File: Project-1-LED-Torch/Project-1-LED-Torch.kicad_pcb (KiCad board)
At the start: 2 copper layers, 4 parts, among them SW1 SW_DPDT_x2

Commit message: do PCB layout design, step 8, setup
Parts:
- moved BT1 4.82 mm to (139.0, 74.5)
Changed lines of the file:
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@@
 	(footprint "Battery:BatteryHolder_Keystone_1058_1x2032"
 		(layer "F.Cu")
-		(at 138.975 79.32397)
+		(at 138.975 74.5)
 		(descr "http://www.keyelco.com/product-pdf.cfm?p=14028")
 		(tags "Keystone type 1058 coin cell retainer")

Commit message: do PCB layout design, steps 9, 10, outline and constraints, footprints
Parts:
- moved D1 90.4 mm to (56.2, 113.2)
- moved SW1 63.2 mm to (73.5, 111.0)
- moved R1 59.2 mm to (69.2, 117.1), turned to 90 degrees
- moved BT1 55.9 mm to (98.8, 113.2)
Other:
- board outline added: 62.5 x 18.5 mm
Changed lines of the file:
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@@
 	(footprint "LED_THT:LED_D5.0mm"
 		(layer "F.Cu")
-		(at 144.785 95.375)
+		(at 56.21 113.25)
 		(descr "LED, diameter 5.0mm, 2 pins, http://cdn-reichelt.de/documents/datenblatt/A500/LL-504BC2E-009.pdf, generated by kicad-footprint-generator")
 		(tags "LED")
@@
 		)
 		(point
-			(at 146.055 95.375)
+			(at 57.48 113.25)
 			(size 2)
 			(layer "F.Fab")
@@
 	(footprint "Button_Switch_THT:SW_TH_Tactile_Omron_B3F-100x"
 		(layer "F.Cu")
-		(at 134.195 93.265)
+		(at 73.5 111)
 		(descr "Tactile switch, 6x6 mm, H4.3 mm, 6.5 mm pitch, https://omronfs.omron.com/en_US/ecb/products/pdf/en-b3f.pdf")
 		(tags "Omron B3F-10xx SPST 1P1T")
@@
 	(footprint "Resistor_THT:R_Axial_DIN0204_L3.6mm_D1.6mm_P7.62mm_Horizontal"
 		(layer "F.Cu")
-		(at 123.475 93.215)
+		(at 69.25 117.06 90)
 		(descr "Resistor, Axial_DIN0204 series, Axial, Horizontal, pin pitch=7.62mm, 0.167W, length*diameter=3.6*1.6mm^2, http://cdn-reichelt.de/documents/datenblatt/B400/1_4W%23YAG.pdf")
 		(tags "Resistor Axial_DIN0204 series Axial Horizontal pin pitch 7.62mm 0.167W length 3.6mm diameter 1.6mm")
 		(property "Reference" "R1"
-			(at 3.81 -1.92 0)
+			(at 3.81 -1.92 90)
 			(layer "F.SilkS")
 			(effects
@@
 		)
 		(property "Value" "R"
-			(at 3.81 1.92 0)
+			(at 3.81 1.92 90)
 			(layer "F.Fab")
 			(effects
@@
 		)
 		(property "Datasheet" ""
-			(at 0 0 0)
+			(at 0 0 90)
 			(layer "F.Fab")
 			(hide yes)
@@
 		)
 		(property "Description" "Resistor"
-			(at 0 0 0)
+			(at 0 0 90)
 			(layer "F.Fab")
 			(hide yes)
@@
 		)
 		(property "KiLib_Generator" "resistor/THT"
-			(at 0 0 0)
+			(at 0 0 90)
 			(layer "F.SilkS")
 			(hide yes)
@@
 		(duplicate_pad_numbers_are_jumpers no)
 		(fp_line
+			(start 6.68 0)
+			(end 5.73 0)
+			(stroke
+				(width 0.12)
+				(type solid)
+			)
+			(layer "F.SilkS")
+		)
+		(fp_line
 			(start 0.94 0)
 			(end 1.89 0)
-			(stroke
-				(width 0.12)
-				(type solid)
-			)
-			(layer "F.SilkS")
-		)
-		(fp_line
-			(start 6.68 0)
-			(end 5.73 0)
 			(stroke
 				(width 0.12)
@@
 		)
 		(fp_line
+			(start 7.62 0)
+			(end 5.61 0)
+			(stroke
+				(width 0.1)
+				(type solid)
+			)
+			(layer "F.Fab")
+		)
+		(fp_line
 			(start 0 0)
 			(end 2.01 0)
-			(stroke
-				(width 0.1)
-				(type solid)
-			)
-			(layer "F.Fab")
-		)
-		(fp_line
-			(start 7.62 0)
-			(end 5.61 0)
 			(stroke
 				(width 0.1)
@@
 		)
 		(fp_text user "${REFERENCE}"
-			(at 3.81 0 0)
+			(at 3.81 0 90)
 			(layer "F.Fab")
 			(effects
@@
 		)
 		(pad "1" thru_hole circle
-			(at 0 0)
+			(at 0 0 90)
 			(size 1.4 1.4)
 			(drill 0.7)
@@
 		)
 		(pad "2" thru_hole circle
-			(at 7.62 0)
+			(at 7.62 0 90)
 			(size 1.4 1.4)
 			(drill 0.7)
@@
 	(footprint "Battery:BatteryHolder_Keystone_1058_1x2032"
 		(layer "F.Cu")
-		(at 138.975 74.5)
+		(at 98.75 113.25)
 		(descr "http://www.keyelco.com/product-pdf.cfm?p=14028")
 		(tags "Keystone type 1058 coin cell retainer")
@@
 		)
 	)
+	(gr_rect
+		(start 53.5 104)
+		(end 116 122.5)
+		(stroke
+			(width 0.05)
+			(type default)
+		)
+		(fill no)
+		(layer "Edge.Cuts")
+	)
+	(gr_circle
+		(center 63.5 113.25)
+		(end 65 113.25)
+		(stroke
+			(width 0.05)
+			(type default)
+		)
+		(fill no)
+		(layer "Edge.Cuts")
+	)
 	(embedded_fonts no)

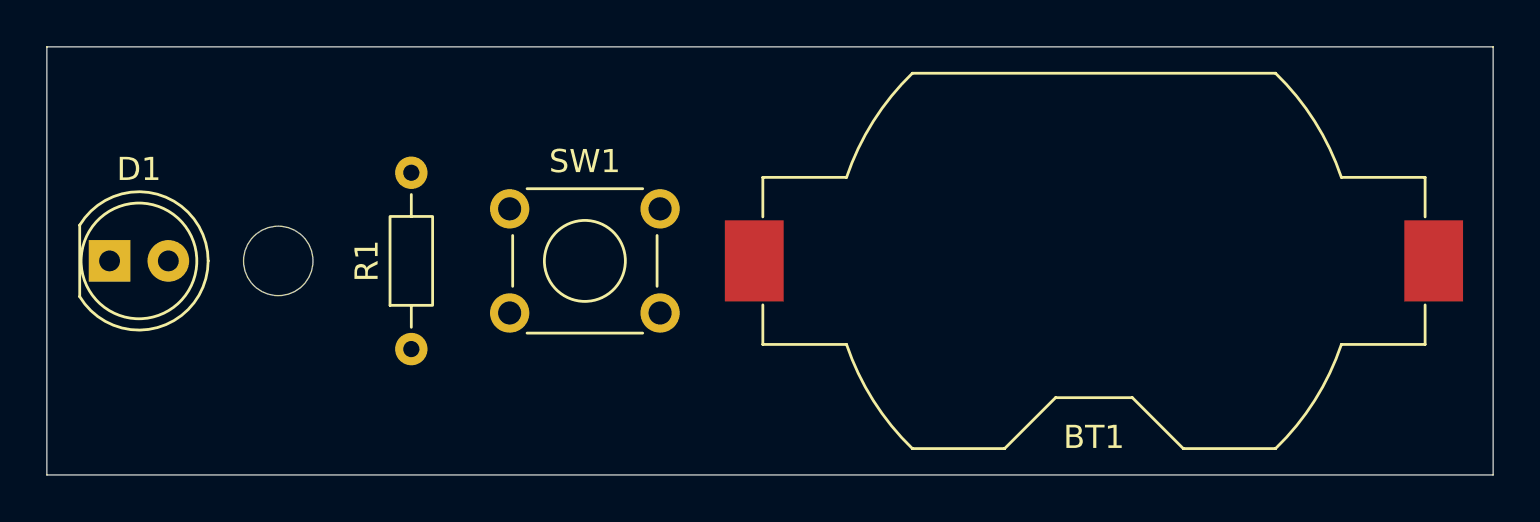
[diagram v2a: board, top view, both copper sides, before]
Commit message: minor update PCB layout design, steps 9, 10, outline and constraints, footprints
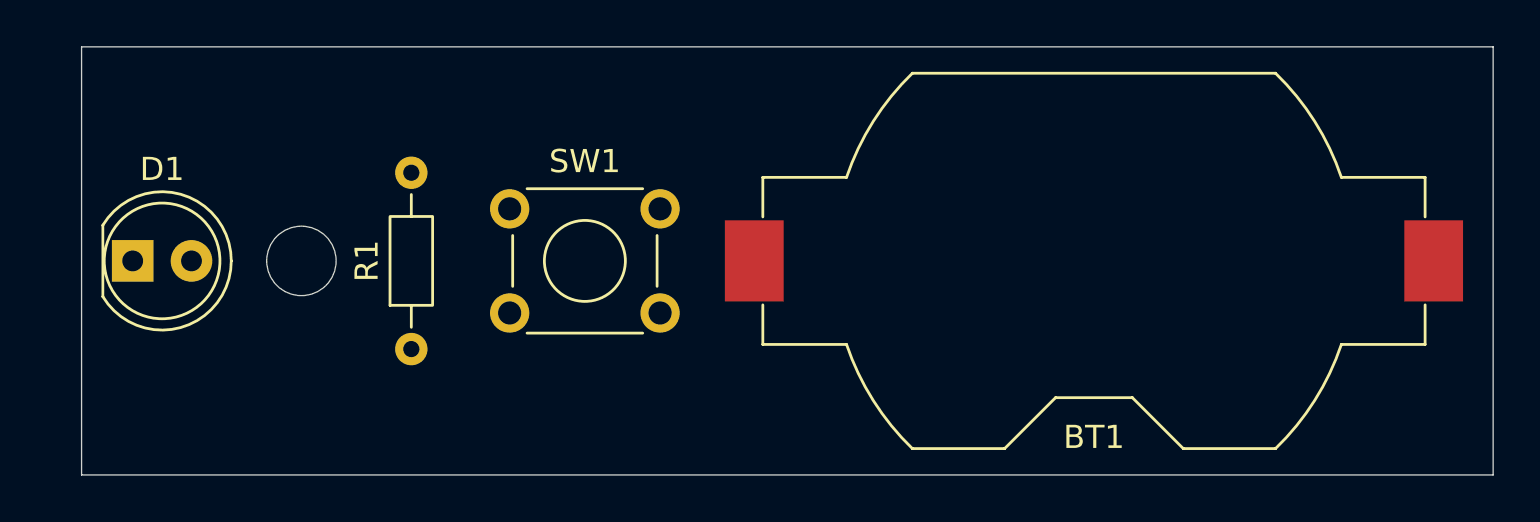
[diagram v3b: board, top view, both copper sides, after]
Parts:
- moved D1 1.00 mm to (57.2, 113.2)
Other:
- board size 62.5 x 18.5 mm -> 61 x 18.5 mm
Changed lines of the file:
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@@
 	(footprint "LED_THT:LED_D5.0mm"
 		(layer "F.Cu")
-		(at 56.21 113.25)
+		(at 57.21 113.25)
 		(descr "LED, diameter 5.0mm, 2 pins, http://cdn-reichelt.de/documents/datenblatt/A500/LL-504BC2E-009.pdf, generated by kicad-footprint-generator")
 		(tags "LED")
@@
 		)
 		(point
-			(at 57.48 113.25)
+			(at 58.48 113.25)
 			(size 2)
 			(layer "F.Fab")
@@
 	)
 	(gr_rect
-		(start 53.5 104)
+		(start 55 104)
 		(end 116 122.5)
 		(stroke
@@
 	)
 	(gr_circle
-		(center 63.5 113.25)
-		(end 65 113.25)
+		(center 64.5 113.25)
+		(end 66 113.25)
 		(stroke
 			(width 0.05)

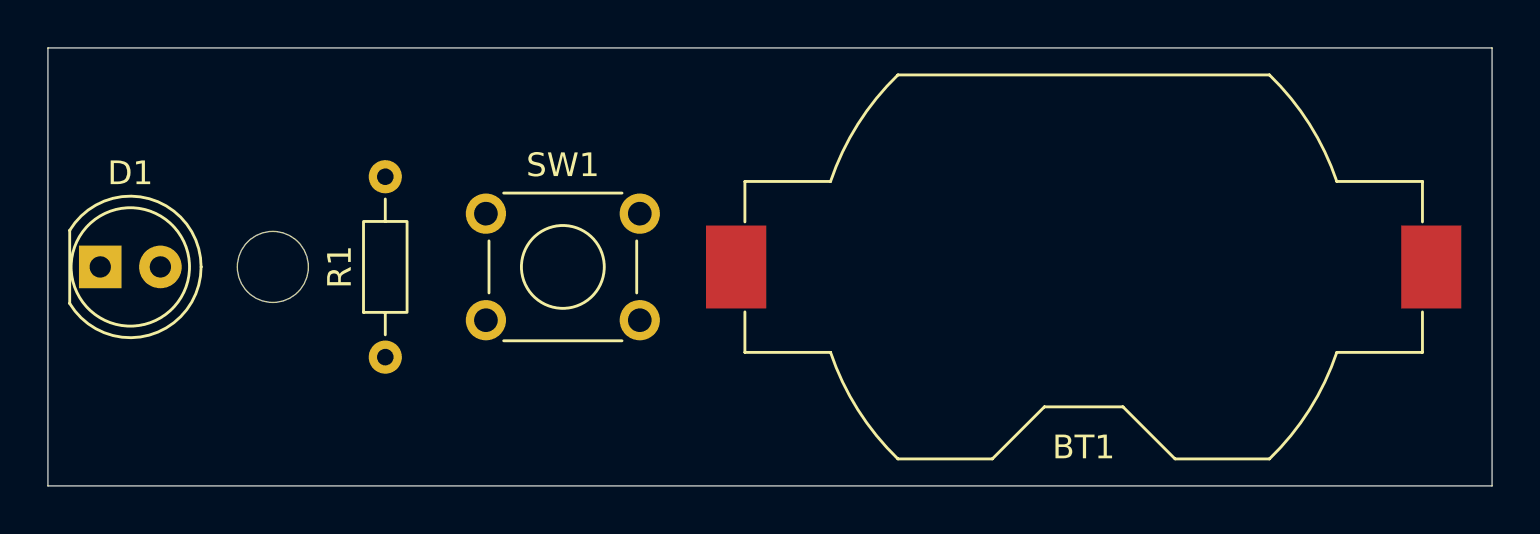
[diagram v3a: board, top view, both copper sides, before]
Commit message: do PCB layout design, step 11, route
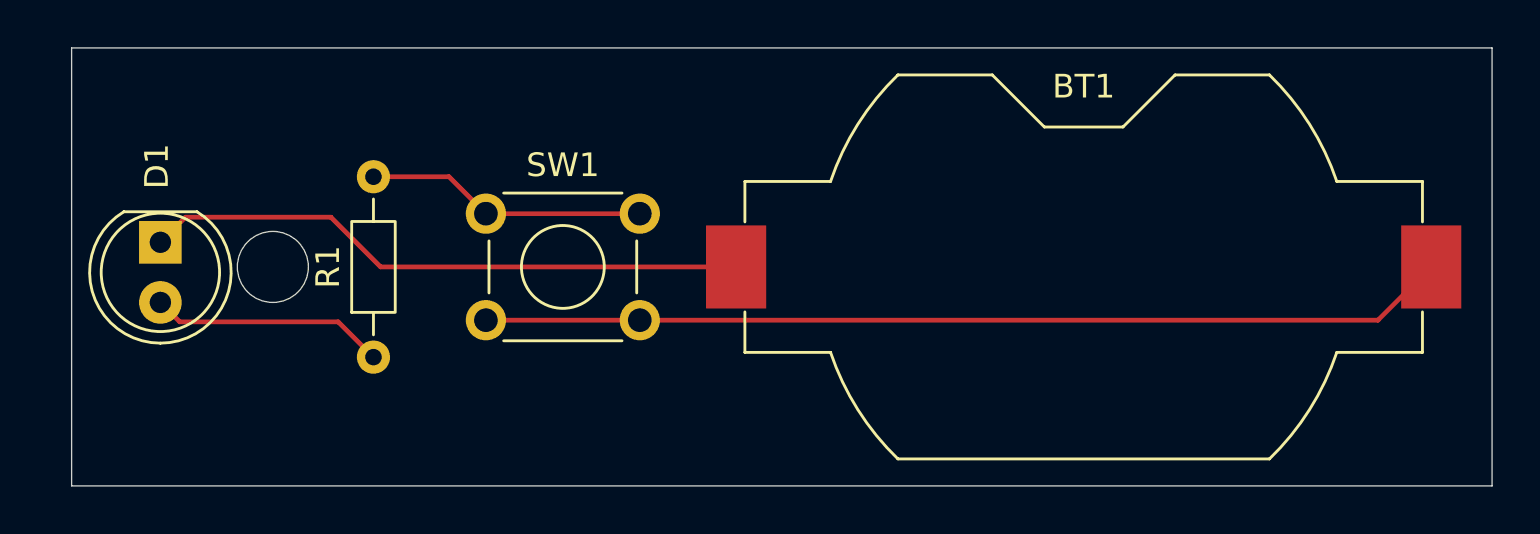
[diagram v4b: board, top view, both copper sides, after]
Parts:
- moved D1 2.74 mm to (59.8, 112.2), turned to -90 degrees
- moved R1 0.50 mm to (68.8, 117.1)
- turned BT1 to 180 degrees
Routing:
- net /Battery_positive: track 0.00 -> 40.9 mm
- net /LED_cathode: track 0.00 -> 25.6 mm
- net Net-(SW1A-A): track 0.00 -> 11.9 mm
- net /LED_anode: track 0.00 -> 9.96 mm
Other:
- board size 61 x 18.5 mm -> 60 x 18.5 mm

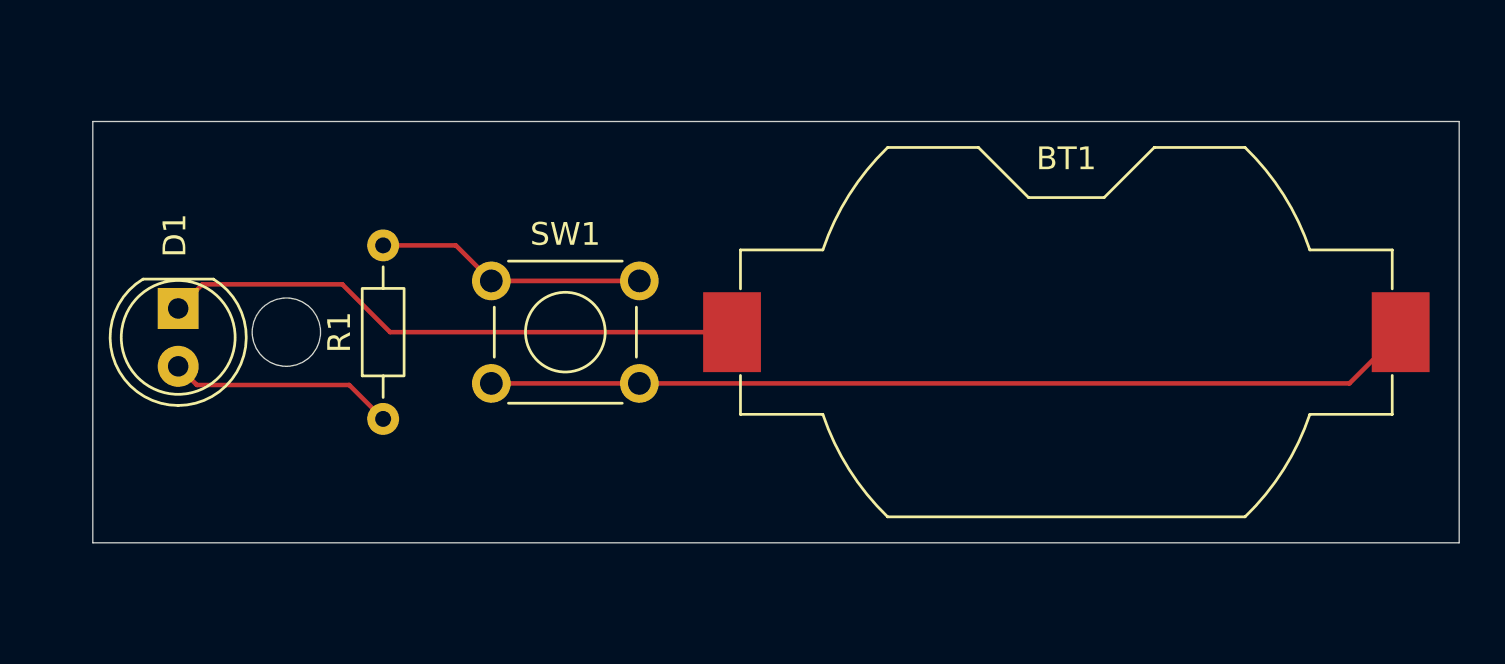
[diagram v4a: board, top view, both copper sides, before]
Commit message: update PCB layout design, steps 9 11, outline, route
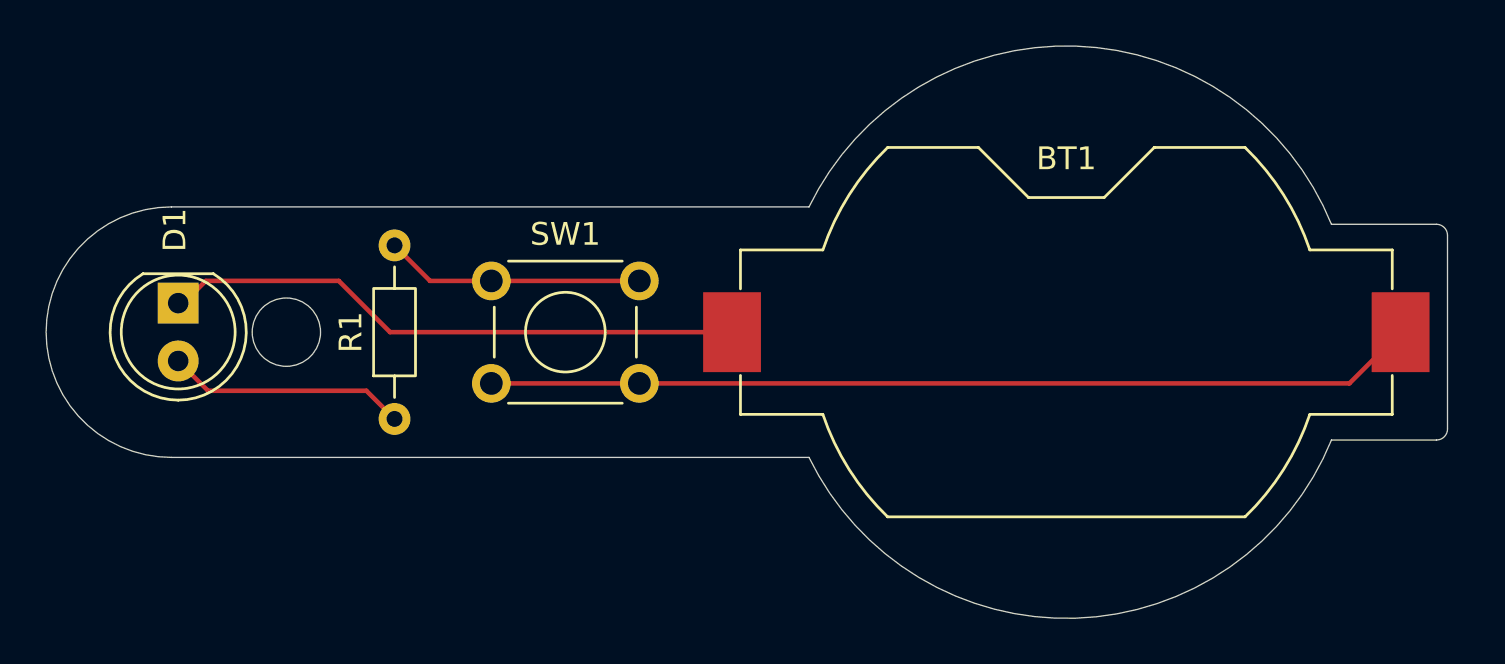
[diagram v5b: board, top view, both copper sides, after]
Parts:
- moved R1 0.50 mm to (69.2, 117.1)
- moved D1 0.23 mm to (59.8, 112.0)
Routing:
- net /LED_anode: track 9.96 -> 10.6 mm
- net Net-(SW1A-A): track 11.9 -> 11.4 mm
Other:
- board size 60 x 18.5 mm -> 61.5 x 25.1 mm
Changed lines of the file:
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@@
 	(footprint "LED_THT:LED_D5.0mm"
 		(layer "F.Cu")
-		(at 59.75 112.21 -90)
+		(at 59.75 111.975 -90)
 		(descr "LED, diameter 5.0mm, 2 pins, http://cdn-reichelt.de/documents/datenblatt/A500/LL-504BC2E-009.pdf, generated by kicad-footprint-generator")
 		(tags "LED")
@@
 		)
 		(point
-			(at 59.75 113.48)
+			(at 59.75 113.245)
 			(size 2)
 			(layer "F.Fab")
@@
 	(footprint "Resistor_THT:R_Axial_DIN0204_L3.6mm_D1.6mm_P7.62mm_Horizontal"
 		(layer "F.Cu")
-		(at 68.75 117.06 90)
+		(at 69.25 117.06 90)
 		(descr "Resistor, Axial_DIN0204 series, Axial, Horizontal, pin pitch=7.62mm, 0.167W, length*diameter=3.6*1.6mm^2, http://cdn-reichelt.de/documents/datenblatt/B400/1_4W%23YAG.pdf")
 		(tags "Resistor Axial_DIN0204 series Axial Horizontal pin pitch 7.62mm 0.167W length 3.6mm diameter 1.6mm")
@@
 		)
 	)
-	(gr_rect
-		(start 56 104)
-		(end 116 122.5)
+	(gr_line
+		(start 59.45 107.75)
+		(end 87.45 107.75)
 		(stroke
 			(width 0.05)
 			(type default)
 		)
-		(fill no)
+		(locked yes)
+		(layer "Edge.Cuts")
+	)
+	(gr_arc
+		(start 59.45 118.75)
+		(mid 53.95 113.25)
+		(end 59.45 107.75)
+		(stroke
+			(width 0.05)
+			(type default)
+		)
+		(locked yes)
+		(layer "Edge.Cuts")
+	)
+	(gr_line
+		(start 59.45 118.75)
+		(end 87.45 118.75)
+		(stroke
+			(width 0.05)
+			(type default)
+		)
+		(locked yes)
 		(layer "Edge.Cuts")
 	)
@@
 		(layer "Edge.Cuts")
 	)
+	(gr_arc
+		(start 87.45 107.75)
+		(mid 99.167845 100.68953)
+		(end 110.390545 108.513155)
+		(stroke
+			(width 0.05)
+			(type default)
+		)
+		(locked yes)
+		(layer "Edge.Cuts")
+	)
+	(gr_line
+		(start 110.390545 108.513155)
+		(end 115 108.513155)
+		(stroke
+			(width 0.05)
+			(type default)
+		)
+		(locked yes)
+		(layer "Edge.Cuts")
+	)
+	(gr_arc
+		(start 110.390545 117.986845)
+		(mid 99.167845 125.81047)
+		(end 87.45 118.75)
+		(stroke
+			(width 0.05)
+			(type default)
+		)
+		(locked yes)
+		(layer "Edge.Cuts")
+	)
+	(gr_line
+		(start 110.390545 117.986845)
+		(end 115 117.986845)
+		(stroke
+			(width 0.05)
+			(type default)
+		)
+		(locked yes)
+		(layer "Edge.Cuts")
+	)
+	(gr_arc
+		(start 115 108.513155)
+		(mid 115.344251 108.655749)
+		(end 115.486845 109)
+		(stroke
+			(width 0.05)
+			(type default)
+		)
+		(locked yes)
+		(layer "Edge.Cuts")
+	)
+	(gr_line
+		(start 115.486845 109)
+		(end 115.486845 117.5)
+		(stroke
+			(width 0.05)
+			(type default)
+		)
+		(locked yes)
+		(layer "Edge.Cuts")
+	)
+	(gr_arc
+		(start 115.486845 117.5)
+		(mid 115.344251 117.844251)
+		(end 115 117.986845)
+		(stroke
+			(width 0.05)
+			(type default)
+		)
+		(locked yes)
+		(layer "Edge.Cuts")
+	)
 	(segment
-		(start 60.81 111.15)
-		(end 66.954 111.15)
+		(start 60.962 110.998)
+		(end 66.802 110.998)
+		(width 0.2)
+		(layer "F.Cu")
+		(net "/LED_cathode")
+	)
+	(segment
+		(start 66.802 110.998)
+		(end 69.054 113.25)
 		(width 0.2)
 		(layer "F.Cu")
@@
 	(segment
 		(start 59.75 112.21)
-		(end 60.81 111.15)
-		(width 0.2)
-		(layer "F.Cu")
-		(net "/LED_cathode")
-	)
-	(segment
-		(start 66.954 111.15)
-		(end 69.054 113.25)
+		(end 60.962 110.998)
 		(width 0.2)
 		(layer "F.Cu")
@@
 	)
 	(segment
-		(start 60.57 115.57)
-		(end 67.26 115.57)
+		(start 68.014 115.824)
+		(end 69.25 117.06)
 		(width 0.2)
 		(layer "F.Cu")
@@
 	)
 	(segment
-		(start 59.75 114.75)
-		(end 60.57 115.57)
+		(start 61.059 115.824)
+		(end 68.014 115.824)
 		(width 0.2)
 		(layer "F.Cu")
@@
 	)
 	(segment
-		(start 67.26 115.57)
-		(end 68.75 117.06)
+		(start 59.75 114.515)
+		(end 61.059 115.824)
 		(width 0.2)
 		(layer "F.Cu")
@@
 	)
 	(segment
-		(start 68.75 109.44)
-		(end 71.94 109.44)
+		(start 73.5 111)
+		(end 70.81 111)
 		(width 0.2)
 		(layer "F.Cu")
@@
 	)
 	(segment
-		(start 71.94 109.44)
-		(end 73.5 111)
+		(start 70.81 111)
+		(end 69.25 109.44)
 		(width 0.2)
 		(layer "F.Cu")

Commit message: do PCB layout design, step 12, silkscreen
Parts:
- added REF**: KiCad-Logo2_5mm_SilkScreen, Symbol:KiCad-Logo2_5mm_SilkScreen, B.Cu at (98.5, 109.0)
- BT1: value Battery_Cell -> Battery_Cell_2032
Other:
- board text added: "+"
- board text added: "-"
- board text added: "Version 1.0"
